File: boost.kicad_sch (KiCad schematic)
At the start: 4 parts, among them U5 TPS61379QWRTERQ1

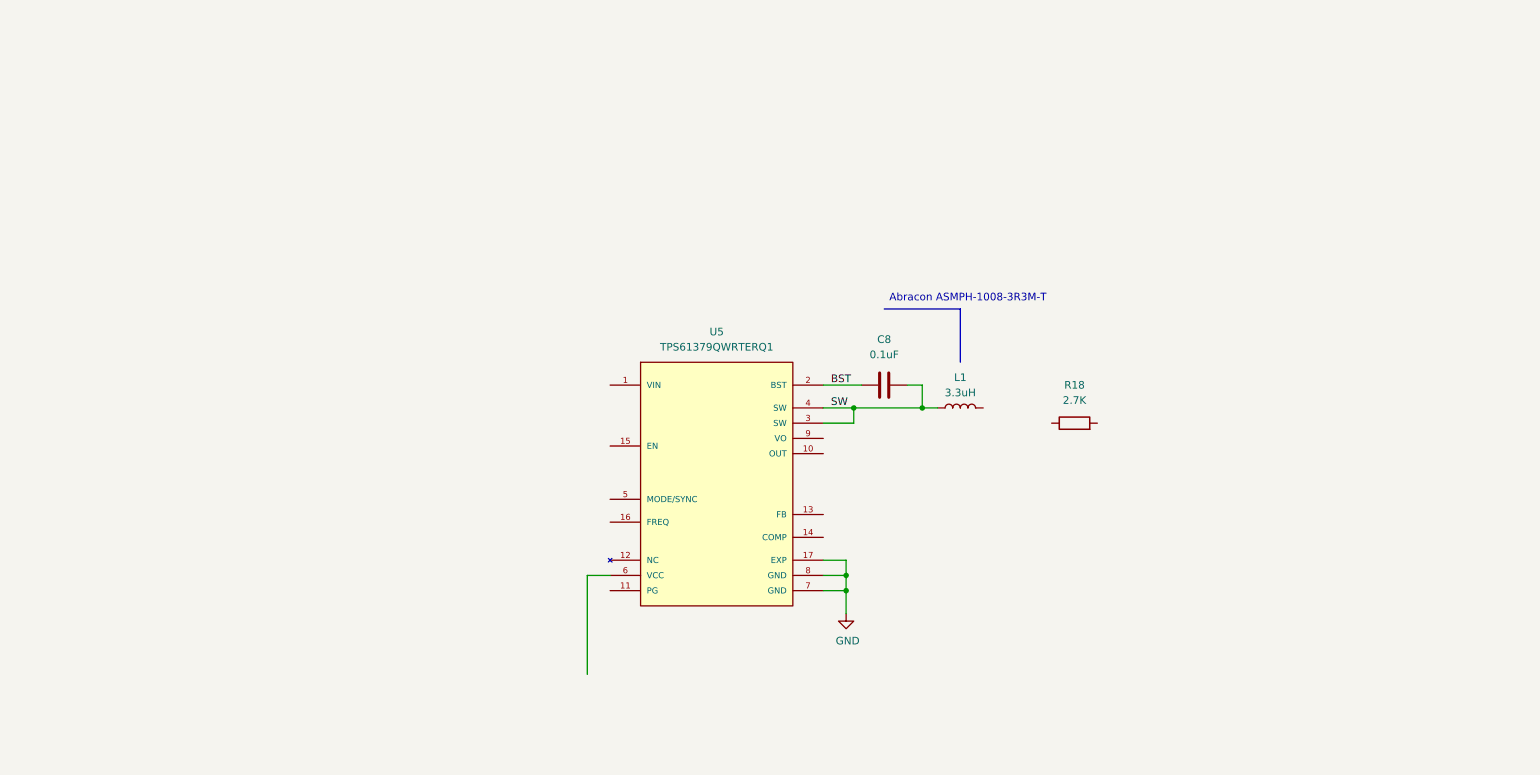
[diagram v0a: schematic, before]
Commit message: Implemented boost stage and now working on schematics for current buffers and rail splitter.
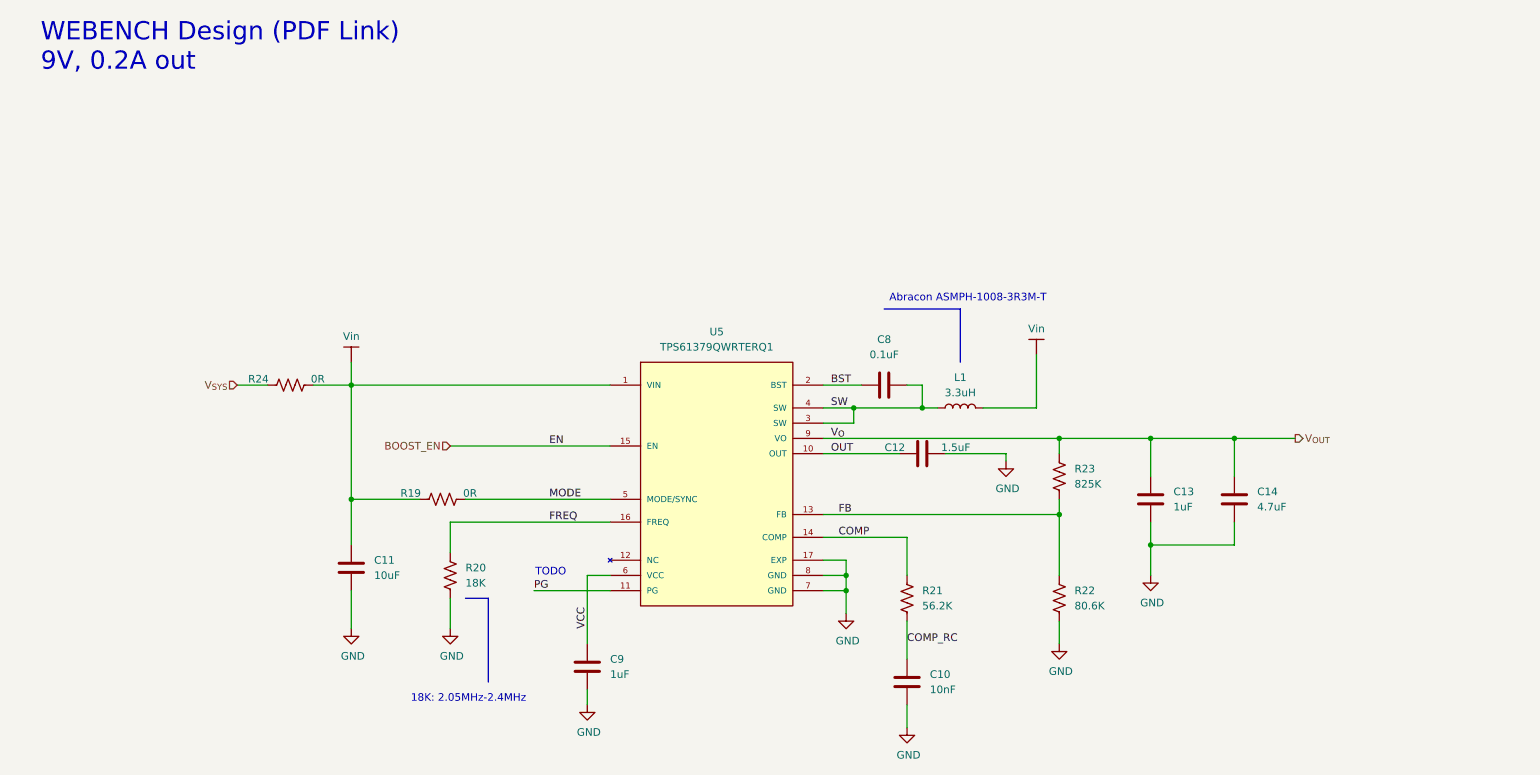
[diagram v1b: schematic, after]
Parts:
- removed R18: 2.7K, symbol Device:R
- added C10: 10nF, symbol Device:C
- added C11: 10uF, symbol Device:C
- added C12: 1.5uF, symbol Device:C
- added C13, C9: 1uF, symbol Device:C
- added C14: 4.7uF, symbol Device:C
- added R19, R24: 0R, symbol Device:R_US
- added R20: 18K, symbol Device:R_US
- added R21: 56.2K, symbol Device:R_US
- added R22: 80.6K, symbol Device:R_US
- added R23: 825K, symbol Device:R_US
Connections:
- net GND: now also C10.2, C11.1, C12.2, C13.1, C14.1, C9.2, R20.1, R22.1
- net Vin: now reaches L1.2
- net Vin: now also U5.1 (VIN), C11.2, R19.1, R24.2
- net OUT: now reaches U5.10 (OUT)
- net OUT: now also C12.1
- net PG: now reaches U5.11 (PG)
- net FB: now reaches U5.13 (FB)
- net FB: now also R22.2, R23.1
- net COMP: now reaches U5.14 (COMP)
- net COMP: now also R21.2
- net BOOST_EN: now reaches U5.15 (EN)
- net FREQ: now reaches U5.16 (FREQ)
- net FREQ: now also R20.2
- net MODE: now reaches U5.5 (MODE/SYNC)
- net MODE: now also R19.2
- net VCC: now reaches U5.6 (VCC)
- net VCC: now also C9.1
- net V_{OUT}: now reaches U5.9 (VO)
- net V_{OUT}: now also C13.2, C14.2, R23.2
- new net COMP_RC: C10.1, R21.1
- new net V_{SYS}: R24.1
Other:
- note added: "18K: 2.05MHz-2.4MHz"
- note added: "TODO"
- note added: "WEBENCH Design (PDF Link) 9V, 0.2A out"
- title: (none) -> ${PROJECT_NAME}

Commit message: Started working on watchdog circuit.
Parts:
- added SW1: SW_SPST, Connector_JST:JST_SH_BM02B-SRSS-TB_1x02-1MP_P1.00mm_Vertical, symbol Switch:SW_SPST
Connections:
- net V_{OUT}: now also SW1.2 (B), SW1.MP; no longer C13.2, C14.2, R23.2, U5.9 (VO)
- new net V_{O}: C13.2, C14.2, R23.2, SW1.1 (A), SW1.MP, U5.9 (VO)
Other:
- note added: "TODO: Pick switch type (slide? panel/thru?)"
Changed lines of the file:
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@@
+		)
+	)
+	(text "TODO: Pick switch type (slide? panel/thru?)"
+		(exclude_from_sim no)
+		(at 253.746 87.884 0)
+		(effects
+			(font
+				(size 1.27 1.27)
+			)
 		)
 	)
@@
 	)
 	(junction
-		(at 232.41 99.06)
-		(diameter 0)
-		(color 0 0 0 0)
-	)
-	(junction
 		(at 168.91 93.98)
 		(diameter 0)
@@
 	)
 	(junction
+		(at 232.41 99.06)
+		(diameter 0)
+		(color 0 0 0 0)
+	)
+	(junction
 		(at 203.2 99.06)
 		(diameter 0)
@@
 	(wire
 		(pts
+			(xy 252.73 99.06) (xy 270.51 99.06)
+		)
+		(stroke
+			(width 0)
+			(type default)
+		)
+	)
+	(wire
+		(pts
 			(xy 194.31 101.6) (xy 194.31 102.87)
 		)
@@
 		)
 	)
+	(label "SW_OUT"
+		(at 257.81 99.06 0)
+		(effects
+			(font
+				(size 1.27 1.27)
+			)
+			(justify left bottom)
+		)
+	)
 	(label "COMP_RC"
 		(at 177.8 133.35 0)
@@
 	(hierarchical_label "V_{OUT}"
 		(shape output)
-		(at 242.57 99.06 0)
+		(at 270.51 99.06 0)
 		(effects
 			(font
@@
 					(unit 1)
 				)
+			)
+		)
+	)
+	(symbol
+		(lib_id "Switch:SW_SPST")
+		(at 247.65 99.06 0)
+		(unit 1)
+		(body_style 1)
+		(exclude_from_sim no)
+		(in_bom yes)
+		(on_board yes)
+		(in_pos_files yes)
+		(dnp no)
+		(fields_autoplaced yes)
+		(property "Reference" "SW1"
+			(at 247.65 92.71 0)
+			(show_name no)
+			(do_not_autoplace no)
+			(effects
+				(font
+					(size 1.27 1.27)
+				)
+			)
+		)
+		(property "Value" "SW_SPST"
+			(at 247.65 95.25 0)
+			(show_name no)
+			(do_not_autoplace no)
+			(effects
+				(font
+					(size 1.27 1.27)
+				)
+			)
+		)
+		(property "Footprint" "Connector_JST:JST_SH_BM02B-SRSS-TB_1x02-1MP_P1.00mm_Vertical"
+			(at 247.65 99.06 0)
+			(hide yes)
+			(show_name no)
+			(do_not_autoplace no)
+			(effects
+				(font
+					(size 1.27 1.27)
+				)
+			)
+		)
+		(property "Datasheet" ""
+			(at 247.65 99.06 0)
+			(hide yes)
+			(show_name no)
+			(do_not_autoplace no)
+			(effects
+				(font
+					(size 1.27 1.27)
+				)
+			)
+		)
+		(property "Description" "Single Pole Single Throw (SPST) switch"
+			(at 247.65 99.06 0)
+			(hide yes)
+			(show_name no)
+			(do_not_autoplace no)
+			(effects
+				(font
+					(size 1.27 1.27)
+				)
+			)
+		)
+		(pin "1"
+		)
+		(pin "2"
+		)
+		(pin "MP"
+		)
+		(pin "MP"
+		)
+		(instances
+			(project "headphone_amp"
+				(path "/62ffec33-ae93-49a8-bfe6-566578dd8e82/339cf5c4-0941-46e9-ae9d-1b8a36e1ad6a"
+					(reference "SW1")
+					(unit 1)
+				)

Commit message: Finalizing watchdog and boost circuit.
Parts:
- removed SW1: SW_SPST, Connector_JST:JST_SH_BM02B-SRSS-TB_1x02-1MP_P1.00mm_Vertical, symbol Switch:SW_SPST
- added Q1: BSS138, Package_TO_SOT_SMD:SOT-23, symbol Transistor_FET:BSS138
- added R39: 470K, symbol Device:R_US
- added R40: 0R, symbol Device:R_US
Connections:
- net GND: now also Q1.2 (S)
- net Vin: now also R39.1
- net BOOST_EN renamed EN
- net EN: now also Q1.3 (D), R39.2
- new net: Q1.1 (G), R40.2
- new net SHUTDOWN: R40.1
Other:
- note removed: "TODO: Pick switch type (slide? panel/thru?)"

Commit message: First rough draft of schematics complete -- missing a lot of PLM/Inventree work. Ran through several Claude reviews.
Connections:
- net V_{O} is gone; now on net V_{OUT}: C13.2, C14.2, R23.2, U5.9 (VO)
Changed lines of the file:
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@@
+	)
+	(junction
+		(at 232.41 99.06)
+		(diameter 0)
+		(color 0 0 0 0)
 	)
 	(junction
@@
 	)
 	(junction
-		(at 232.41 99.06)
-		(diameter 0)
-		(color 0 0 0 0)
-	)
-	(junction
 		(at 203.2 99.06)
 		(diameter 0)
@@
 	(wire
 		(pts
-			(xy 252.73 99.06) (xy 270.51 99.06)
-		)
-		(stroke
-			(width 0)
-			(type default)
-		)
-	)
-	(wire
-		(pts
 			(xy 194.31 101.6) (xy 194.31 102.87)
 		)
@@
 	(wire
 		(pts
-			(xy 232.41 99.06) (xy 242.57 99.06)
+			(xy 232.41 99.06) (xy 248.92 99.06)
 		)
 		(stroke
@@
 	(hierarchical_label "V_{OUT}"
 		(shape output)
-		(at 270.51 99.06 0)
-		(effects
-			(font
+		(at 248.92 99.06 0)
+		(effects
+			(font

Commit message: Small tunes and adjustments before Inventree work.
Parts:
- added R53: 100K, Resistor_SMD:R_0402_1005Metric, symbol #inventree_kicad:R_100K_0402_1PCT_0W0625
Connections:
- net PG: now also R53.1
- net Vin: now also R53.2
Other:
- note removed: "TODO"
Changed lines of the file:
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@@
 	(title_block
 		(title "${PROJECT_NAME}")
-		(date "2026-08-25")
+		(date "2026-08-29")
 		(rev "${REVISION}")
 		(comment 1 "${PCBA_IPN}")
-	)
-	(text "TODO"
-		(exclude_from_sim no)
-		(at 118.364 121.412 0)
-		(effects
-			(font
-				(size 1.27 1.27)
-			)
-		)
 	)
 	(text "WEBENCH Design (PDF Link)\n9V, 0.2A out"
@@
 	(text "18K: 2.05MHz-2.4MHz"
 		(exclude_from_sim no)
-		(at 104.648 142.494 0)
+		(at 102.87 141.986 0)
 		(effects
 			(font
@@
 	(wire
 		(pts
+			(xy 115.57 152.4) (xy 147.32 152.4)
+		)
+		(stroke
+			(width 0)
+			(type default)
+		)
+	)
+	(wire
+		(pts
 			(xy 180.34 93.98) (xy 182.88 93.98)
 		)
@@
 		)
 	)
+	(wire
+		(pts
+			(xy 115.57 124.46) (xy 115.57 152.4)
+		)
+		(stroke
+			(width 0)
+			(type default)
+		)
+	)
 	(polyline
 		(pts
@@
 	(wire
 		(pts
+			(xy 147.32 138.43) (xy 147.32 140.97)
+		)
+		(stroke
+			(width 0)
+			(type default)
+		)
+	)
+	(wire
+		(pts
 			(xy 167.64 121.92) (xy 163.83 121.92)
 		)
@@
 		(pts
 			(xy 199.39 85.09) (xy 199.39 93.98)
+		)
+		(stroke
+			(width 0)
+			(type default)
+		)
+	)
+	(wire
+		(pts
+			(xy 147.32 148.59) (xy 147.32 152.4)
 		)
 		(stroke
@@
 	)
 	(symbol
+		(lib_id "#power_symbols:VCC_LOCAL")
+		(at 147.32 138.43 0)
+		(unit 1)
+		(body_style 1)
+		(exclude_from_sim no)
+		(in_bom yes)
+		(on_board yes)
+		(in_pos_files yes)
+		(dnp no)
+		(property "Reference" "#PWR091"
+			(at 147.32 142.24 0)
+			(hide yes)
+			(show_name no)
+			(do_not_autoplace no)
+			(effects
+				(font
+					(size 1.27 1.27)
+				)
+			)
+		)
+		(property "Value" "Vin"
+			(at 147.32 134.112 0)
+			(show_name no)
+			(do_not_autoplace no)
+			(effects
+				(font
+					(size 1.27 1.27)
+				)
+			)
+		)
+		(property "Footprint" ""
+			(at 147.32 138.43 0)
+			(hide yes)
+			(show_name no)
+			(do_not_autoplace no)
+			(effects
+				(font
+					(size 1.27 1.27)
+				)
+			)
+		)
+		(property "Datasheet" ""
+			(at 147.32 138.43 0)
+			(hide yes)
+			(show_name no)
+			(do_not_autoplace no)
+			(effects
+				(font
+					(size 1.27 1.27)
+				)
+			)
+		)
+		(property "Description" "Power symbol creates a local label with name \"+3.3V\""
+			(at 147.32 138.43 0)
+			(hide yes)
+			(show_name no)
+			(do_not_autoplace no)
+			(effects
+				(font
+					(size 1.27 1.27)
+				)
+			)
+		)
+		(pin "1"
+		)
+		(instances
+			(project "headphone_amp"
+				(path "/62ffec33-ae93-49a8-bfe6-566578dd8e82/339cf5c4-0941-46e9-ae9d-1b8a36e1ad6a"
+					(reference "#PWR091")
+					(unit 1)
+				)
+			)
+		)
+	)
+	(symbol
 		(lib_id "power:GND")
 		(at 101.6 130.81 0)
@@
 					(unit 1)
 				)
+			)
+		)
+	)
+	(symbol
+		(lib_id "#inventree_kicad:R_100K_0402_1PCT_0W0625")
+		(at 147.32 144.78 180)
+		(unit 1)
+		(body_style 1)
+		(exclude_from_sim no)
+		(in_bom yes)
+		(on_board yes)
+		(in_pos_files yes)
+		(dnp no)
+		(fields_autoplaced yes)
+		(property "Reference" "R53"
+			(at 149.86 143.5099 0)
+			(show_name no)
+			(do_not_autoplace no)
+			(effects
+				(font
+					(size 1.27 1.27)
+				)
+				(justify right)
+			)
+		)
+		(property "Value" "100K"
+			(at 149.86 146.0499 0)
+			(show_name no)
+			(do_not_autoplace no)
+			(effects
+				(font
+					(size 1.27 1.27)
+				)
+				(justify right)
+			)
+		)
+		(property "Footprint" "Resistor_SMD:R_0402_1005Metric"
+			(at 146.304 144.526 90)
+			(hide yes)
+			(show_name no)
+			(do_not_autoplace no)
+			(effects
+				(font
+					(size 1.27 1.27)
+				)
+			)
+		)
+		(property "Datasheet" ""
+			(at 147.32 144.78 0)
+			(hide yes)
+			(show_name no)
+			(do_not_autoplace no)
+			(effects
+				(font
+					(size 1.27 1.27)
+				)
+			)
+		)
+		(property "Description" "100 kOhms ±1% 0.063W, 1/16W Chip Resistor 0402 (1005 Metric)"
+			(at 147.32 144.78 0)
+			(hide yes)
+			(show_name no)
+			(do_not_autoplace no)
+			(effects
+				(font
+					(size 1.27 1.27)
+				)
+			)
+		)
+		(property "IPN" "302-0008"
+			(at 147.32 144.78 0)
+			(hide yes)
+			(show_name no)
+			(do_not_autoplace no)
+			(effects
+				(font
+					(size 1.27 1.27)
+				)
+			)
+		)
+		(property "InvenTree" "23"
+			(at 147.32 144.78 0)
+			(hide yes)
+			(show_name no)
+			(do_not_autoplace no)
+			(effects
+				(font
+					(size 1.27 1.27)
+				)
+			)
+		)
+		(property "Part URL" "http://10.0.0.33/web/part/23/"
+			(at 147.32 144.78 0)
+			(hide yes)
+			(show_name no)
+			(do_not_autoplace no)
+			(effects
+				(font
+					(size 1.27 1.27)
+				)
+			)
+		)
+		(pin "2"
+		)
+		(pin "1"
+		)
+		(instances
+			(project "headphone_amp"
+				(path "/62ffec33-ae93-49a8-bfe6-566578dd8e82/339cf5c4-0941-46e9-ae9d-1b8a36e1ad6a"
+					(reference "R53")
+					(unit 1)
+				)

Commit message: Started Inventree work.
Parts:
- removed R40: 0R, symbol Device:R_US
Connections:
- net SHUTDOWN: now also Q1.1 (G)
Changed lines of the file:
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@@
-	(wire
-		(pts
-			(xy 54.61 111.76) (xy 58.42 111.76)
-		)
-		(stroke
-			(width 0)
-			(type default)
-		)
-	)
 	(wire
 		(pts
@@
 	(wire
 		(pts
-			(xy 41.91 111.76) (xy 46.99 111.76)
+			(xy 41.91 111.76) (xy 58.42 111.76)
 		)
 		(stroke
@@
 					(unit 1)
 				)
-			)
-		)
-	)
-	(symbol
-		(lib_id "Device:R_US")
-		(at 50.8 111.76 90)
-		(unit 1)
-		(body_style 1)
-		(exclude_from_sim no)
-		(in_bom yes)
-		(on_board yes)
-		(in_pos_files yes)
-		(dnp no)
-		(property "Reference" "R40"
-			(at 45.466 110.744 90)
-			(show_name no)
-			(do_not_autoplace no)
-			(effects
-				(font
-					(size 1.27 1.27)
-				)
-			)
-		)
-		(property "Value" "0R"
-			(at 55.372 110.744 90)
-			(show_name no)
-			(do_not_autoplace no)
-			(effects
-				(font
-					(size 1.27 1.27)
-				)
-			)
-		)
-		(property "Footprint" ""
-			(at 51.054 110.744 90)
-			(hide yes)
-			(show_name no)
-			(do_not_autoplace no)
-			(effects
-				(font
-					(size 1.27 1.27)
-				)
-			)
-		)
-		(property "Datasheet" ""
-			(at 50.8 111.76 0)
-			(hide yes)
-			(show_name no)
-			(do_not_autoplace no)
-			(effects
-				(font
-					(size 1.27 1.27)
-				)
-			)
-		)
-		(property "Description" "Resistor, US symbol"
-			(at 50.8 111.76 0)
-			(hide yes)
-			(show_name no)
-			(do_not_autoplace no)
-			(effects
-				(font
-					(size 1.27 1.27)
-				)
-			)
-		)
-		(pin "2"
-		)
-		(pin "1"
-		)
-		(instances
-			(project "headphone_amp"
-				(path "/62ffec33-ae93-49a8-bfe6-566578dd8e82/339cf5c4-0941-46e9-ae9d-1b8a36e1ad6a"
-					(reference "R40")
-					(unit 1)
-				)

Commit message: Corrected issues Claude identified, added 'poor man's cab filter' on recovery stage per Ihsan.
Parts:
- added R55: 1M, Resistor_SMD:R_0402_1005Metric, symbol #inventree_kicad:R_1M_0402_1PCT_0W0625
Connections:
- net EN: now also R55.2
- net GND: now also R55.1
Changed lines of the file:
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@@
+	)
+	(junction
+		(at 66.04 100.33)
+		(diameter 0)
+		(color 0 0 0 0)
 	)
 	(junction
@@
 	(wire
 		(pts
+			(xy 44.45 100.33) (xy 49.53 100.33)
+		)
+		(stroke
+			(width 0)
+			(type default)
+		)
+	)
+	(wire
+		(pts
 			(xy 128.27 121.92) (xy 124.46 121.92)
 		)
@@
 	(wire
 		(pts
+			(xy 57.15 100.33) (xy 66.04 100.33)
+		)
+		(stroke
+			(width 0)
+			(type default)
+		)
+	)
+	(wire
+		(pts
 			(xy 190.5 93.98) (xy 199.39 93.98)
 		)
@@
 		(pts
 			(xy 163.83 93.98) (xy 168.91 93.98)
+		)
+		(stroke
+			(width 0)
+			(type default)
+		)
+	)
+	(wire
+		(pts
+			(xy 44.45 102.87) (xy 44.45 100.33)
 		)
 		(stroke
@@
 	)
 	(symbol
+		(lib_id "power:GND")
+		(at 44.45 102.87 0)
+		(unit 1)
+		(body_style 1)
+		(exclude_from_sim no)
+		(in_bom yes)
+		(on_board yes)
+		(in_pos_files yes)
+		(dnp no)
+		(property "Reference" "#PWR095"
+			(at 44.45 109.22 0)
+			(hide yes)
+			(show_name no)
+			(do_not_autoplace no)
+			(effects
+				(font
+					(size 1.27 1.27)
+				)
+			)
+		)
+		(property "Value" "GND"
+			(at 44.704 107.442 0)
+			(show_name no)
+			(do_not_autoplace no)
+			(effects
+				(font
+					(size 1.27 1.27)
+				)
+			)
+		)
+		(property "Footprint" ""
+			(at 44.45 102.87 0)
+			(hide yes)
+			(show_name no)
+			(do_not_autoplace no)
+			(effects
+				(font
+					(size 1.27 1.27)
+				)
+			)
+		)
+		(property "Datasheet" ""
+			(at 44.45 102.87 0)
+			(hide yes)
+			(show_name no)
+			(do_not_autoplace no)
+			(effects
+				(font
+					(size 1.27 1.27)
+				)
+			)
+		)
+		(property "Description" "Power symbol creates a global label with name \"GND\" , ground"
+			(at 44.45 102.87 0)
+			(hide yes)
+			(show_name no)
+			(do_not_autoplace no)
+			(effects
+				(font
+					(size 1.27 1.27)
+				)
+			)
+		)
+		(pin "1"
+		)
+		(instances
+			(project "headphone_amp"
+				(path "/62ffec33-ae93-49a8-bfe6-566578dd8e82/339cf5c4-0941-46e9-ae9d-1b8a36e1ad6a"
+					(reference "#PWR095")
+					(unit 1)
+				)
+			)
+		)
+	)
+	(symbol
 		(lib_id "Device:L")
 		(at 186.69 93.98 90)
@@
 					(unit 1)
 				)
+			)
+		)
+	)
+	(symbol
+		(lib_id "#inventree_kicad:R_1M_0402_1PCT_0W0625")
+		(at 53.34 100.33 90)
+		(unit 1)
+		(body_style 1)
+		(exclude_from_sim no)
+		(in_bom yes)
+		(on_board yes)
+		(in_pos_files yes)
+		(dnp no)
+		(fields_autoplaced yes)
+		(property "Reference" "R55"
+			(at 53.34 93.98 90)
+			(show_name no)
+			(do_not_autoplace no)
+			(effects
+				(font
+					(size 1.27 1.27)
+				)
+			)
+		)
+		(property "Value" "1M"
+			(at 53.34 96.52 90)
+			(show_name no)
+			(do_not_autoplace no)
+			(effects
+				(font
+					(size 1.27 1.27)
+				)
+			)
+		)
+		(property "Footprint" "Resistor_SMD:R_0402_1005Metric"
+			(at 53.594 99.314 90)
+			(hide yes)
+			(show_name no)
+			(do_not_autoplace no)
+			(effects
+				(font
+					(size 1.27 1.27)
+				)
+			)
+		)
+		(property "Datasheet" ""
+			(at 53.34 100.33 0)
+			(hide yes)
+			(show_name no)
+			(do_not_autoplace no)
+			(effects
+				(font
+					(size 1.27 1.27)
+				)
+			)
+		)
+		(property "Description" "1 MOhms ±1% 0.063W, 1/16W Chip Resistor 0402 (1005 Metric) Moisture Resistant Thick Film"
+			(at 53.34 100.33 0)
+			(hide yes)
+			(show_name no)
+			(do_not_autoplace no)
+			(effects
+				(font
+					(size 1.27 1.27)
+				)
+			)
+		)
+		(property "IPN" "302-0007"
+			(at 53.34 100.33 0)
+			(hide yes)
+			(show_name no)
+			(do_not_autoplace no)
+			(effects
+				(font
+					(size 1.27 1.27)
+				)
+			)
+		)
+		(property "InvenTree" "22"
+			(at 53.34 100.33 0)
+			(hide yes)
+			(show_name no)
+			(do_not_autoplace no)
+			(effects
+				(font
+					(size 1.27 1.27)
+				)
+			)
+		)
+		(property "Part URL" "http://10.0.0.33/web/part/22/"
+			(at 53.34 100.33 0)
+			(hide yes)
+			(show_name no)
+			(do_not_autoplace no)
+			(effects
+				(font
+					(size 1.27 1.27)
+				)
+			)
+		)
+		(pin "2"
+		)
+		(pin "1"
+		)
+		(instances
+			(project "headphone_amp"
+				(path "/62ffec33-ae93-49a8-bfe6-566578dd8e82/339cf5c4-0941-46e9-ae9d-1b8a36e1ad6a"
+					(reference "R55")
+					(unit 1)
+				)
